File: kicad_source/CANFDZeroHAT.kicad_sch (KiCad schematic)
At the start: 32 parts, among them CN1 RASPI-IO

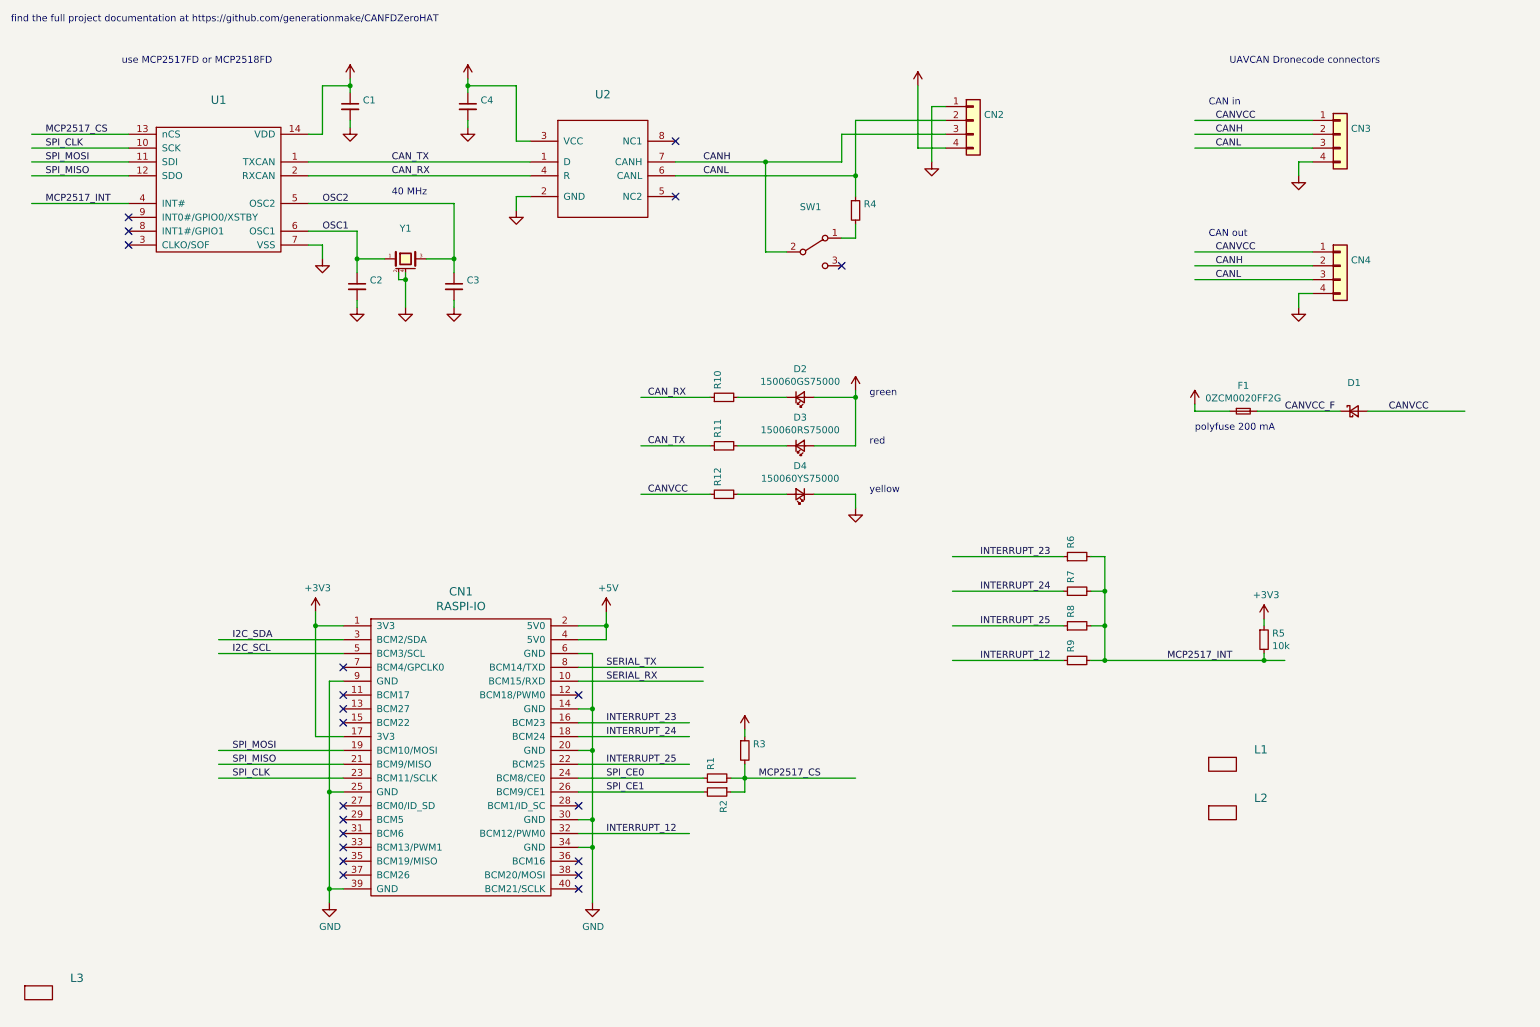
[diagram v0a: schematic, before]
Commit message: added mounting pad on CAN connector
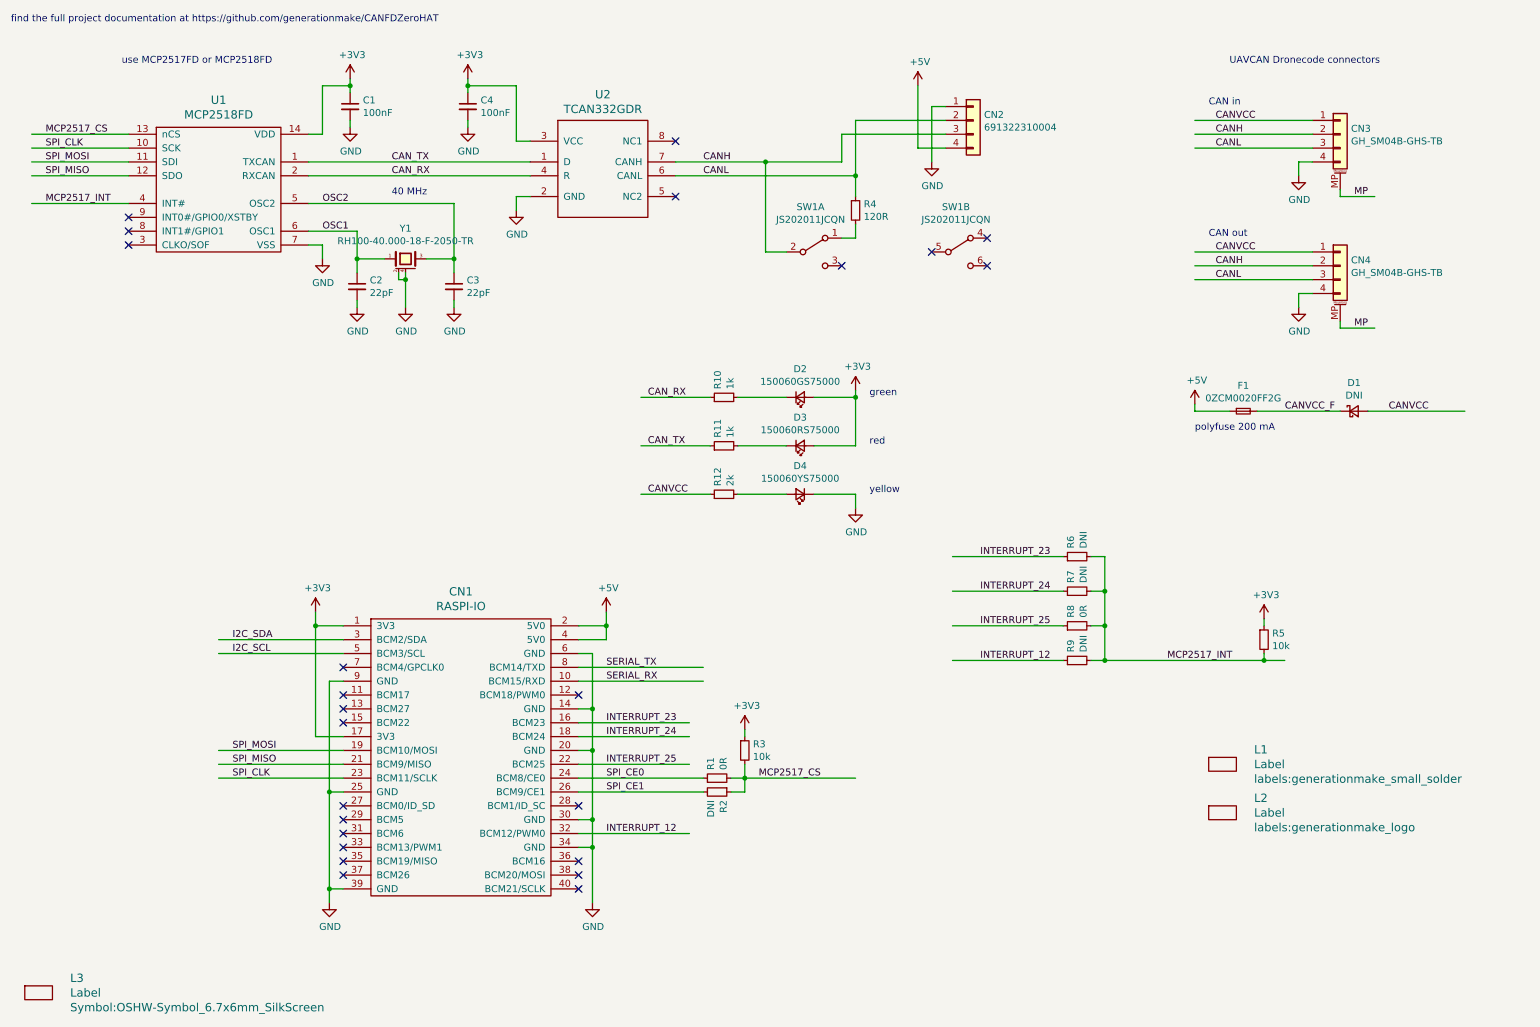
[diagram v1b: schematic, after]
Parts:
- added unit 2 of SW1
- C1, C4: value (none) -> 100nF; footprint (none) -> capacitors:C_0603
- C2, C3: value (none) -> 22pF; footprint (none) -> capacitors:C_0603
- CN2: value (none) -> 691322310004; footprint (none) -> CON_wuerth:WR-TBL_691322310004
- CN3, CN4: value (none) -> GH_SM04B-GHS-TB; footprint (none) -> Connector_JST:JST_GH_SM04B-GHS-TB_1x04-1MP_P1.25mm_Horizontal; symbol Connector_Generic:Conn_01x04 -> Connector_Generic_MountingPin:Conn_01x04_MountingPin
- D1: value (none) -> DNI; footprint (none) -> diodes:SOD-123
- L1: value (none) -> Label; footprint (none) -> labels:generationmake_small_solder
- L2: value (none) -> Label; footprint (none) -> labels:generationmake_logo
- L3: value (none) -> Label; footprint (none) -> Symbol:OSHW-Symbol_6.7x6mm_SilkScreen
- R1, R8: value (none) -> 0R; footprint (none) -> resistors:R_0603
- R10, R11: value (none) -> 1k; footprint (none) -> resistors:R_0603
- R12: value (none) -> 2k; footprint (none) -> resistors:R_0603
- R2, R6, R7, R9: value (none) -> DNI; footprint (none) -> resistors:R_0603
- R3: value (none) -> 10k; footprint (none) -> resistors:R_0603
- R4: value (none) -> 120R; footprint (none) -> resistors:R_0603
- SW1: value (none) -> JS202011JCQN; footprint (none) -> mechanical-switches:CK_JS202011JCQN; symbol Switch:SW_SPDT -> Switch:SW_DPDT_x2
- U1: value (none) -> MCP2518FD; footprint (none) -> SOIC:SOIC-14_3.9x8.7mm_Pitch1.27mm
- U2: value (none) -> TCAN332GDR; footprint (none) -> SOIC:SOIC-8_3.9x4.9mm_Pitch1.27mm
- Y1: value (none) -> RH100-40.000-18-F-2050-TR; footprint (none) -> crystals:Crystal_SMD_3.2x2.5mm_4Pad
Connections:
- new net MP: CN3.MP (MountPin), CN4.MP (MountPin)
- no-connect marks 21 -> 24

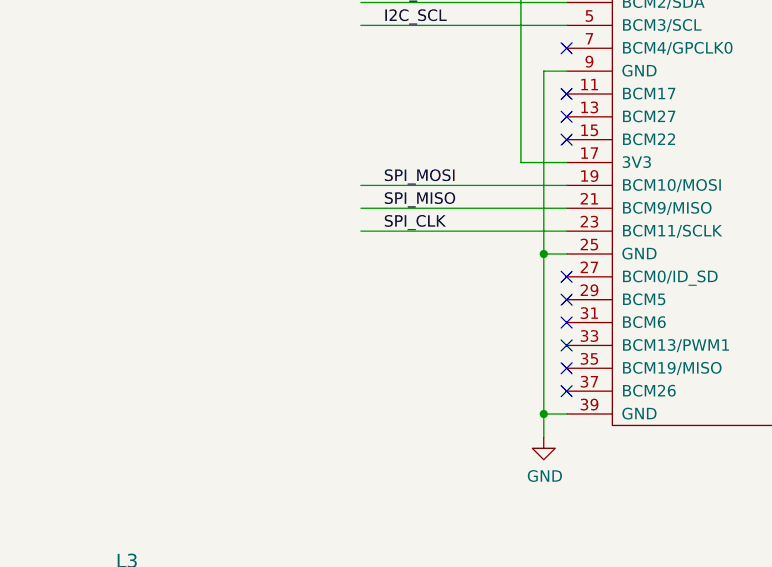
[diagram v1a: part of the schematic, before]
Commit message: updated footprints, added pulldown on SDO
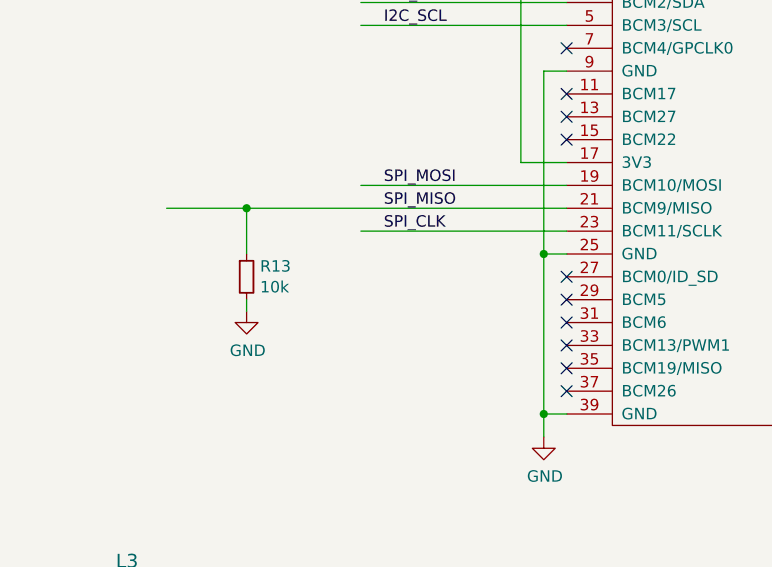
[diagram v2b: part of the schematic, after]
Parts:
- added R13: 10k, Resistor_SMD:R_0603_1608Metric, symbol Device:R_Small
- C1, C2, C3, C4: footprint capacitors:C_0603 -> Capacitor_SMD:C_0603_1608Metric
- D1: footprint diodes:SOD-123 -> Diode_SMD:D_SOD-123
- D2, D3, D4: footprint LEDs:LED_0603 -> LED_SMD:LED_0603_1608Metric
- F1, R1, R10, R11, R12, R2, R3, R4, R5, R6, R7, R8, R9: footprint resistors:R_0603 -> Resistor_SMD:R_0603_1608Metric
- U1: footprint SOIC:SOIC-14_3.9x8.7mm_Pitch1.27mm -> Package_SO:SOIC-14_3.9x8.7mm_P1.27mm
- U2: footprint SOIC:SOIC-8_3.9x4.9mm_Pitch1.27mm -> Package_SO:SOIC-8_3.9x4.9mm_P1.27mm
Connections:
- net GND: now also R13.2
- net SPI_MISO: now also R13.1

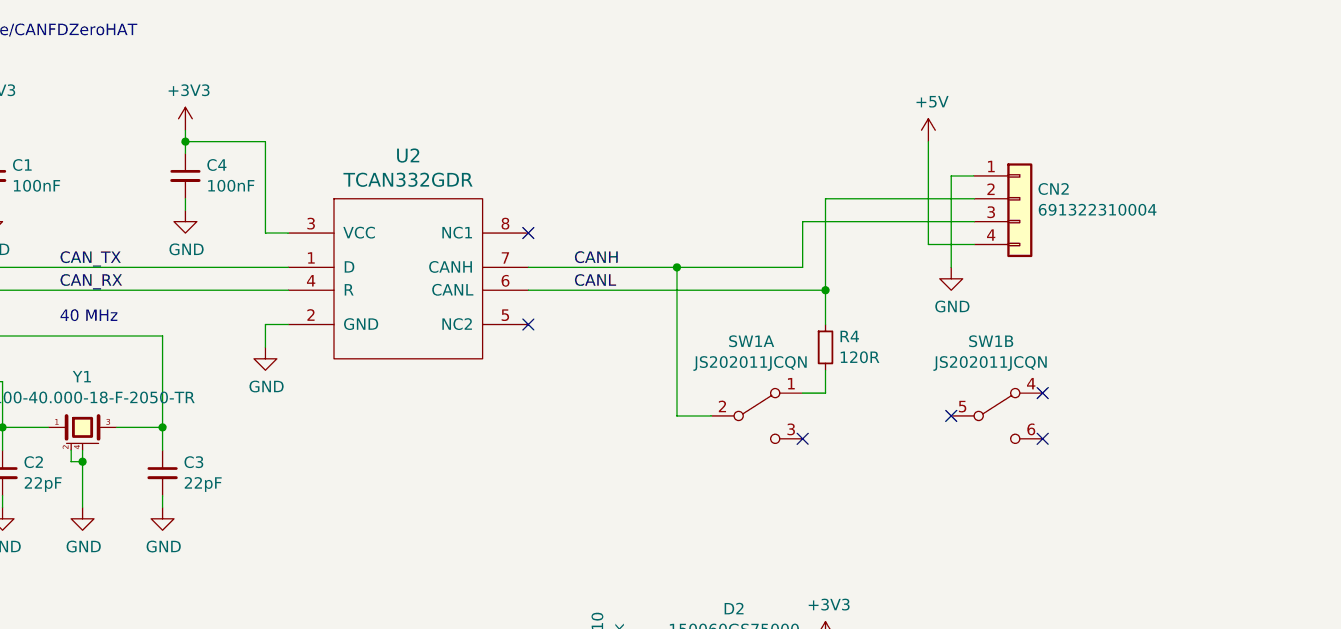
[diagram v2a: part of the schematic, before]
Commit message: updated symbol of CAN driver
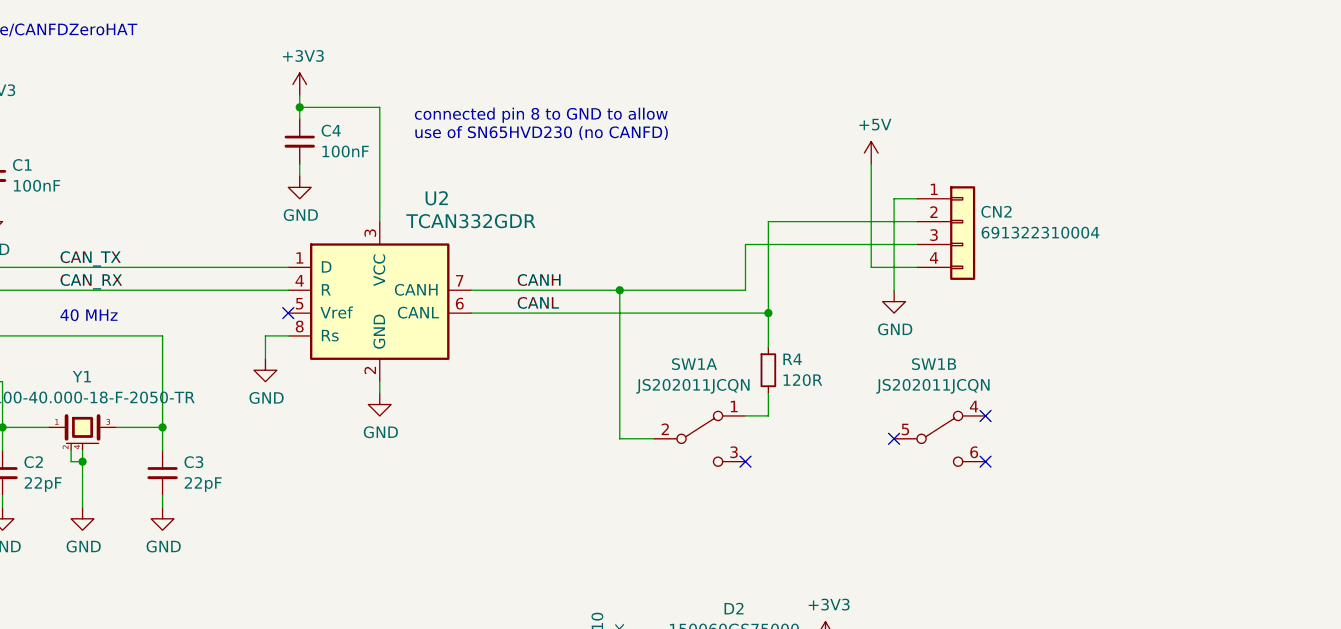
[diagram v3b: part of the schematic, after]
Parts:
- U2: symbol CANFDZeroHAT-rescue:SN65HVD232-CAN-transceiver -> Interface_CAN_LIN:SN65HVD230
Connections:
- net GND: now also U2.8 (Rs)
- no-connect marks 24 -> 23
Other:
- note added: "connected pin 8 to GND to allow use of SN65HVD230 (no CANFD)"
- moved on the sheet: C4, CN2, R4, SW1A, SW1B

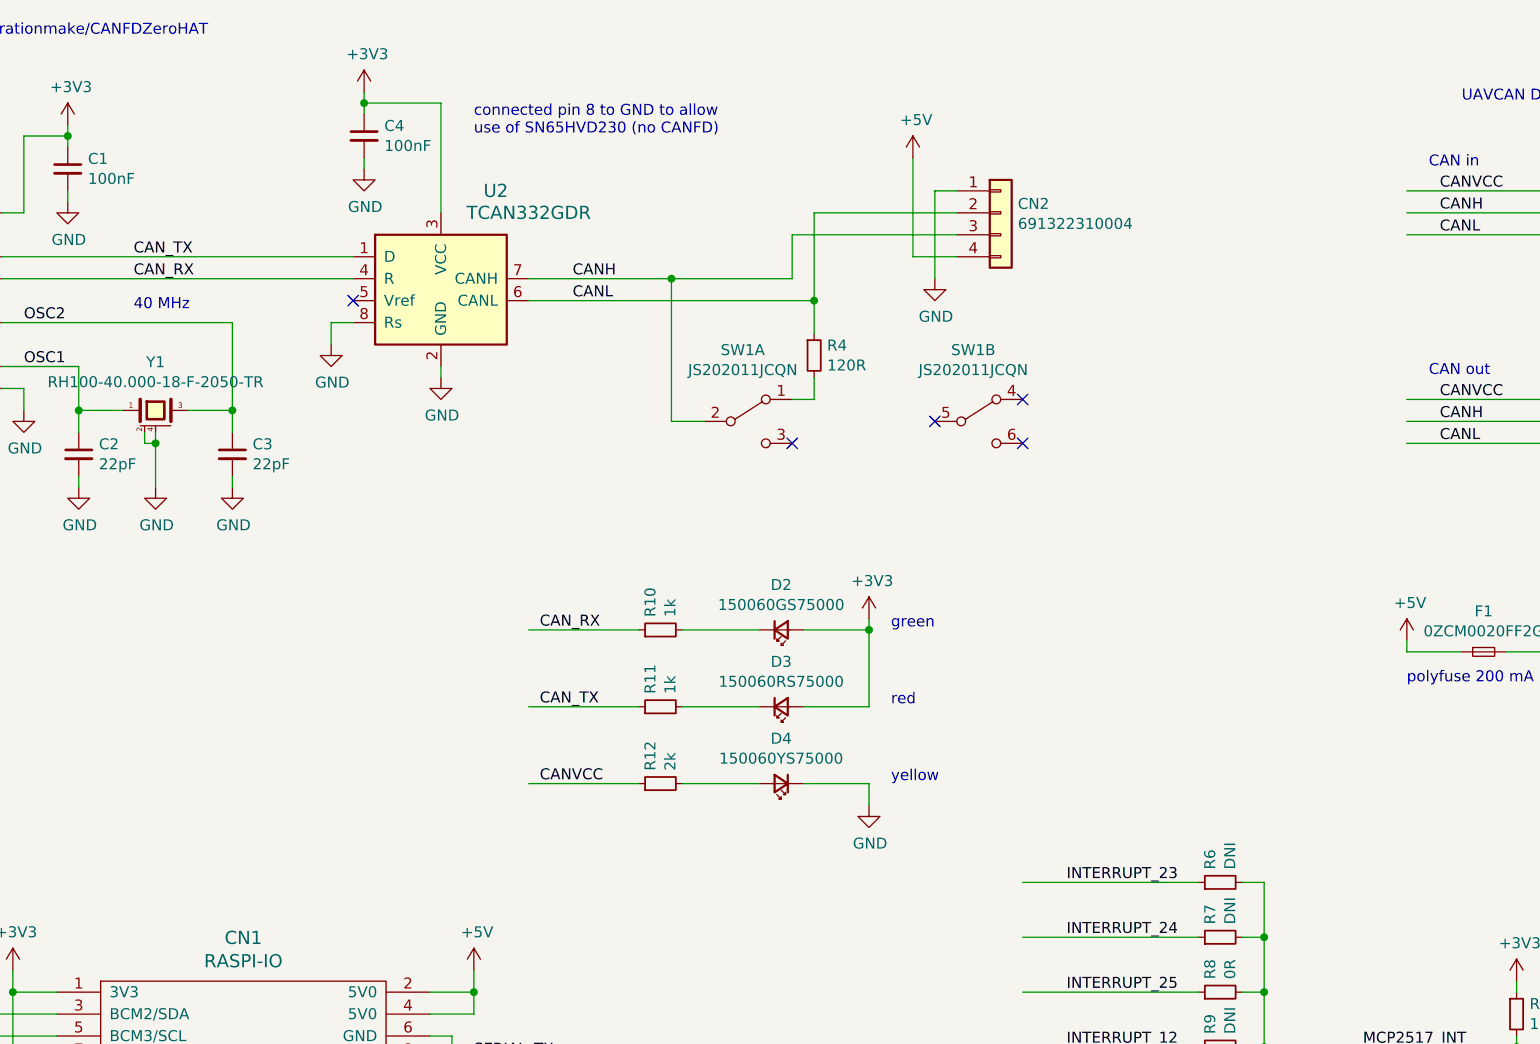
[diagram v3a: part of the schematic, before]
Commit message: added protection on CAN, updated schematic pdf
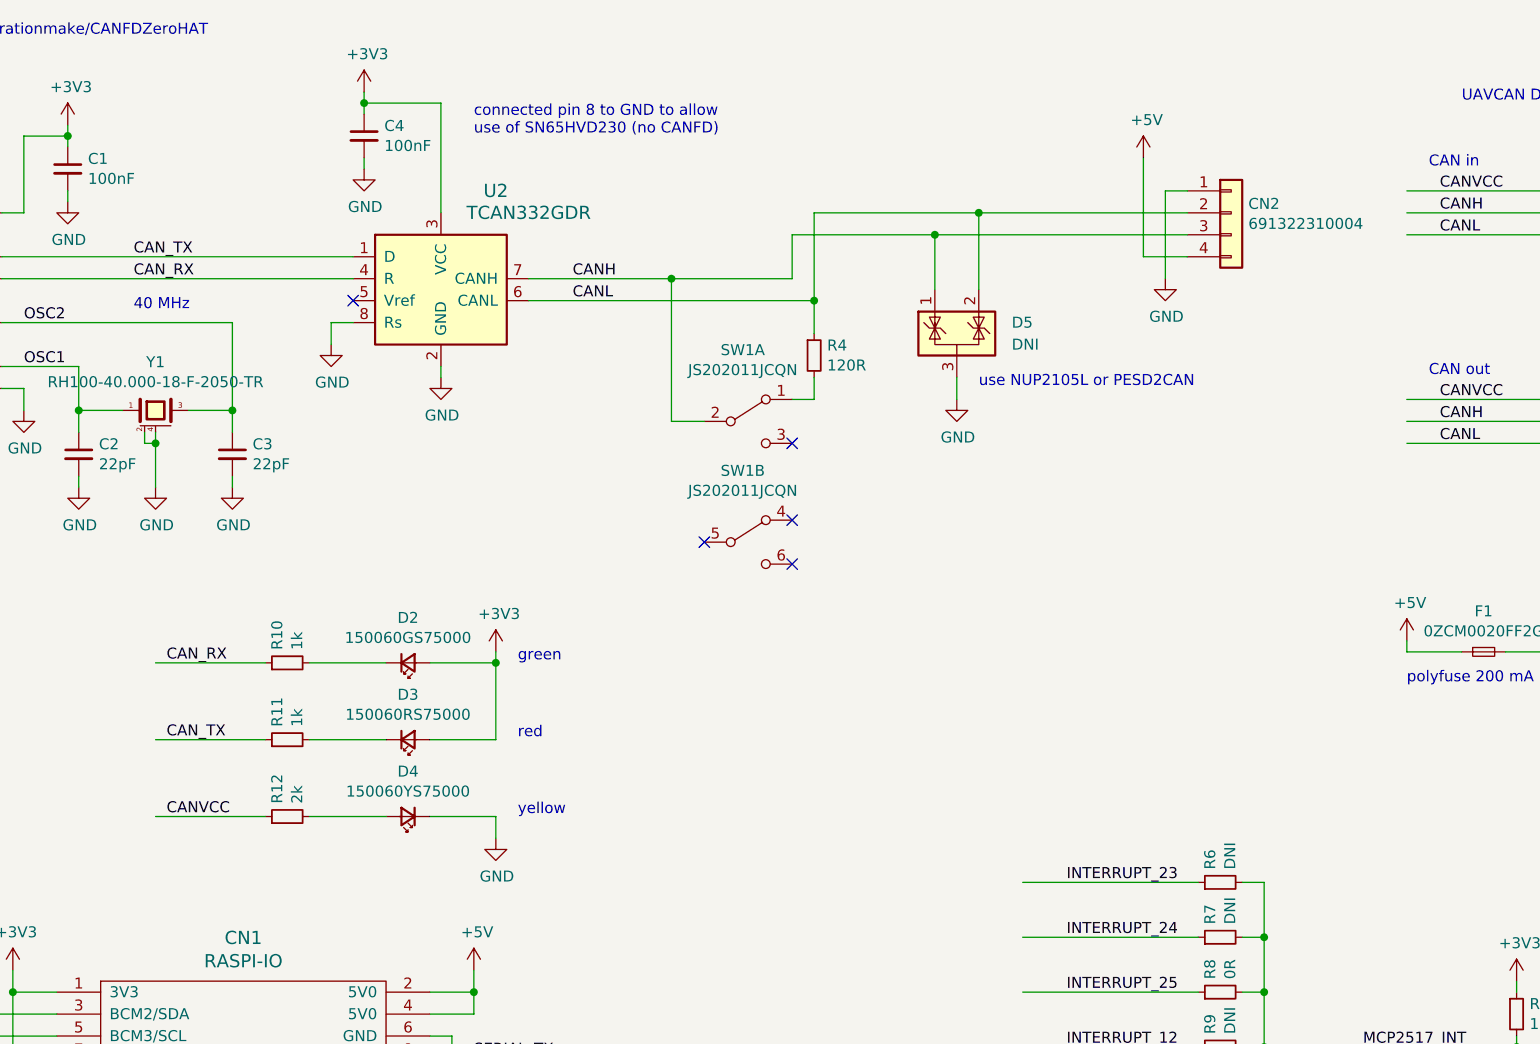
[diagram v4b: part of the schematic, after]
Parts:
- added D5: DNI, Package_TO_SOT_SMD:SOT-23, symbol Power_Protection:NUP2105L
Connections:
- net CANH: now also D5.1 (K)
- net CANL: now also D5.2 (K)
- net GND: now also D5.3 (A)
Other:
- note added: "use NUP2105L or PESD2CAN"
- moved on the sheet: CN2, D2, D3, D4, R10, R11, R12, SW1B
